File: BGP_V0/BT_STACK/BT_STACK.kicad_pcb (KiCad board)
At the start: 2 copper layers, 30 x 30 mm, 13 parts, among them P1 CONN_01X05, U1 OPA180

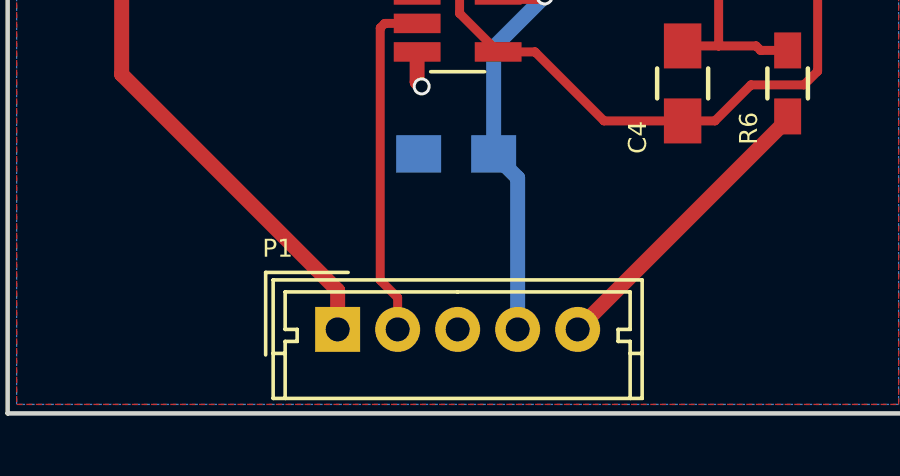
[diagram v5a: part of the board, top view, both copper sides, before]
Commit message: Slight changes to Port layer placement - gerbers done
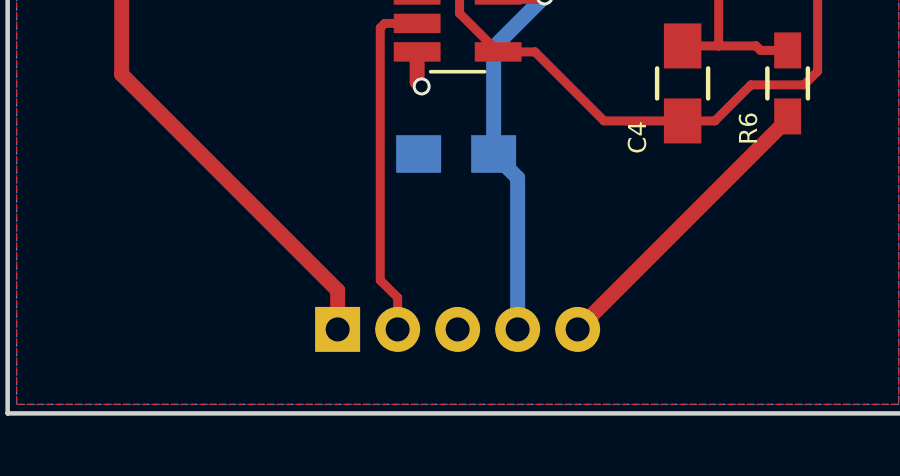
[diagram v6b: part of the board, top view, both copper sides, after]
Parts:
- P1: moved to B.Cu
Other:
- board text added: "+"
- board text added: "-"
- board text added: "G"
- board text added: "I"
- board text added: "O"
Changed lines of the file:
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@@
-(kicad_pcb (version 4) (host pcbnew 4.0.7)
+(kicad_pcb (version 4) (host pcbnew 4.0.4-1.fc24-product)
   (general
     (links 22)
     (no_connects 0)
-    (area 169.924999 67.424999 200.075001 99.455)
+    (area 169.924999 67.424999 200.075001 98.075001)
     (thickness 1.6)
-    (drawings 9)
+    (drawings 14)
     (tracks 80)
     (zones 0)
@@
     )
   )
-  (module Connectors_Molex:Molex_MicroLatch-53253-0570_05x2.00mm_Straight (layer F.Cu)
+  (module Connectors_Molex:Molex_MicroLatch-53253-0570_05x2.00mm_Straight (layer B.Cu)
     (at 181 95.2)
     (descr "Molex Micro-Latch connector, PN:53253-0570, top entry type, through hole")
     (tags "conn molex micro latch")
-    (fp_text reference P1 (at -2 -2.7) (layer F.SilkS)
-      (effects (font (size 0.6 0.6) (thickness 0.15)))
-    )
-    (fp_text value CONN_01X05 (at 4 3.4) (layer F.Fab) hide
-      (effects (font (size 0.6 0.6) (thickness 0.15)))
-    )
-    (fp_line (start -2 -1.5) (end -2 2.15) (layer F.Fab) (width 0.1))
-    (fp_line (start -2 2.15) (end 10 2.15) (layer F.Fab) (width 0.1))
-    (fp_line (start 10 2.15) (end 10 -1.5) (layer F.Fab) (width 0.1))
-    (fp_line (start 10 -1.5) (end -2 -1.5) (layer F.Fab) (width 0.1))
-    (fp_line (start -2.6 -2.1) (end -2.6 2.75) (layer F.CrtYd) (width 0.05))
-    (fp_line (start -2.6 2.75) (end 10.65 2.75) (layer F.CrtYd) (width 0.05))
-    (fp_line (start 10.65 2.75) (end 10.65 -2.1) (layer F.CrtYd) (width 0.05))
-    (fp_line (start 10.65 -2.1) (end -2.6 -2.1) (layer F.CrtYd) (width 0.05))
-    (fp_line (start -2.15 -1.65) (end -2.15 2.3) (layer F.SilkS) (width 0.12))
-    (fp_line (start -2.15 2.3) (end 10.15 2.3) (layer F.SilkS) (width 0.12))
-    (fp_line (start 10.15 2.3) (end 10.15 -1.65) (layer F.SilkS) (width 0.12))
-    (fp_line (start 10.15 -1.65) (end -2.15 -1.65) (layer F.SilkS) (width 0.12))
-    (fp_line (start 0.35 -1.9) (end -2.4 -1.9) (layer F.SilkS) (width 0.12))
-    (fp_line (start -2.4 -1.9) (end -2.4 0.85) (layer F.SilkS) (width 0.12))
-    (fp_line (start 0.35 -1.9) (end -2.4 -1.9) (layer F.Fab) (width 0.1))
-    (fp_line (start -2.4 -1.9) (end -2.4 0.85) (layer F.Fab) (width 0.1))
-    (fp_line (start -2.15 0.8) (end -1.75 0.8) (layer F.SilkS) (width 0.12))
-    (fp_line (start 10.15 0.8) (end 9.75 0.8) (layer F.SilkS) (width 0.12))
-    (fp_line (start 4 -1.25) (end -1.75 -1.25) (layer F.SilkS) (width 0.12))
-    (fp_line (start -1.75 -1.25) (end -1.75 0) (layer F.SilkS) (width 0.12))
-    (fp_line (start -1.75 0) (end -1.35 0) (layer F.SilkS) (width 0.12))
-    (fp_line (start -1.35 0) (end -1.35 0.4) (layer F.SilkS) (width 0.12))
-    (fp_line (start -1.35 0.4) (end -1.75 0.4) (layer F.SilkS) (width 0.12))
-    (fp_line (start -1.75 0.4) (end -1.75 2.3) (layer F.SilkS) (width 0.12))
-    (fp_line (start 4 -1.25) (end 9.75 -1.25) (layer F.SilkS) (width 0.12))
-    (fp_line (start 9.75 -1.25) (end 9.75 0) (layer F.SilkS) (width 0.12))
-    (fp_line (start 9.75 0) (end 9.35 0) (layer F.SilkS) (width 0.12))
-    (fp_line (start 9.35 0) (end 9.35 0.4) (layer F.SilkS) (width 0.12))
-    (fp_line (start 9.35 0.4) (end 9.75 0.4) (layer F.SilkS) (width 0.12))
-    (fp_line (start 9.75 0.4) (end 9.75 2.3) (layer F.SilkS) (width 0.12))
-    (fp_text user %R (at 4 1.5) (layer F.Fab) hide
-      (effects (font (size 0.6 0.6) (thickness 0.15)))
+    (fp_text reference P1 (at 11 -1.85) (layer B.SilkS)
+      (effects (font (size 0.6 0.6) (thickness 0.15)) (justify mirror))
+    )
+    (fp_text value CONN_01X05 (at 4 -3.4) (layer B.Fab) hide
+      (effects (font (size 0.6 0.6) (thickness 0.15)) (justify mirror))
+    )
+    (fp_line (start -2 1.5) (end -2 -2.15) (layer B.Fab) (width 0.1))
+    (fp_line (start -2 -2.15) (end 10 -2.15) (layer B.Fab) (width 0.1))
+    (fp_line (start 10 -2.15) (end 10 1.5) (layer B.Fab) (width 0.1))
+    (fp_line (start 10 1.5) (end -2 1.5) (layer B.Fab) (width 0.1))
+    (fp_line (start -2.6 2.1) (end -2.6 -2.75) (layer B.CrtYd) (width 0.05))
+    (fp_line (start -2.6 -2.75) (end 10.65 -2.75) (layer B.CrtYd) (width 0.05))
+    (fp_line (start 10.65 -2.75) (end 10.65 2.1) (layer B.CrtYd) (width 0.05))
+    (fp_line (start 10.65 2.1) (end -2.6 2.1) (layer B.CrtYd) (width 0.05))
+    (fp_line (start -2.15 1.65) (end -2.15 -2.3) (layer B.SilkS) (width 0.12))
+    (fp_line (start -2.15 -2.3) (end 10.15 -2.3) (layer B.SilkS) (width 0.12))
+    (fp_line (start 10.15 -2.3) (end 10.15 1.65) (layer B.SilkS) (width 0.12))
+    (fp_line (start 10.15 1.65) (end -2.15 1.65) (layer B.SilkS) (width 0.12))
+    (fp_line (start 0.35 1.9) (end -2.4 1.9) (layer B.SilkS) (width 0.12))
+    (fp_line (start -2.4 1.9) (end -2.4 -0.85) (layer B.SilkS) (width 0.12))
+    (fp_line (start 0.35 1.9) (end -2.4 1.9) (layer B.Fab) (width 0.1))
+    (fp_line (start -2.4 1.9) (end -2.4 -0.85) (layer B.Fab) (width 0.1))
+    (fp_line (start -2.15 -0.8) (end -1.75 -0.8) (layer B.SilkS) (width 0.12))
+    (fp_line (start 10.15 -0.8) (end 9.75 -0.8) (layer B.SilkS) (width 0.12))
+    (fp_line (start 4 1.25) (end -1.75 1.25) (layer B.SilkS) (width 0.12))
+    (fp_line (start -1.75 1.25) (end -1.75 0) (layer B.SilkS) (width 0.12))
+    (fp_line (start -1.75 0) (end -1.35 0) (layer B.SilkS) (width 0.12))
+    (fp_line (start -1.35 0) (end -1.35 -0.4) (layer B.SilkS) (width 0.12))
+    (fp_line (start -1.35 -0.4) (end -1.75 -0.4) (layer B.SilkS) (width 0.12))
+    (fp_line (start -1.75 -0.4) (end -1.75 -2.3) (layer B.SilkS) (width 0.12))
+    (fp_line (start 4 1.25) (end 9.75 1.25) (layer B.SilkS) (width 0.12))
+    (fp_line (start 9.75 1.25) (end 9.75 0) (layer B.SilkS) (width 0.12))
+    (fp_line (start 9.75 0) (end 9.35 0) (layer B.SilkS) (width 0.12))
+    (fp_line (start 9.35 0) (end 9.35 -0.4) (layer B.SilkS) (width 0.12))
+    (fp_line (start 9.35 -0.4) (end 9.75 -0.4) (layer B.SilkS) (width 0.12))
+    (fp_line (start 9.75 -0.4) (end 9.75 -2.3) (layer B.SilkS) (width 0.12))
+    (fp_text user %R (at 4 -1.5) (layer B.Fab) hide
+      (effects (font (size 0.6 0.6) (thickness 0.15)) (justify mirror))
     )
     (pad 1 thru_hole rect (at 0 0) (size 1.5 1.5) (drill 0.8) (layers *.Cu *.Mask)
@@
     )
   )
+  (gr_text O (at 189 92) (layer B.SilkS)
+    (effects (font (size 0.6 0.6) (thickness 0.15)) (justify mirror))
+  )
+  (gr_text + (at 187 92) (layer B.SilkS)
+    (effects (font (size 0.6 0.6) (thickness 0.15)) (justify mirror))
+  )
+  (gr_text G (at 185.05 92) (layer B.SilkS)
+    (effects (font (size 0.6 0.6) (thickness 0.15)) (justify mirror))
+  )
+  (gr_text - (at 183 92) (layer B.SilkS)
+    (effects (font (size 0.6 0.6) (thickness 0.15)) (justify mirror))
+  )
+  (gr_text I (at 180.5 92) (layer B.SilkS)
+    (effects (font (size 0.6 0.6) (thickness 0.15)) (justify mirror))
+  )
   (gr_text "BGP V0.0\nB/T Stack" (at 196 70) (layer B.SilkS)

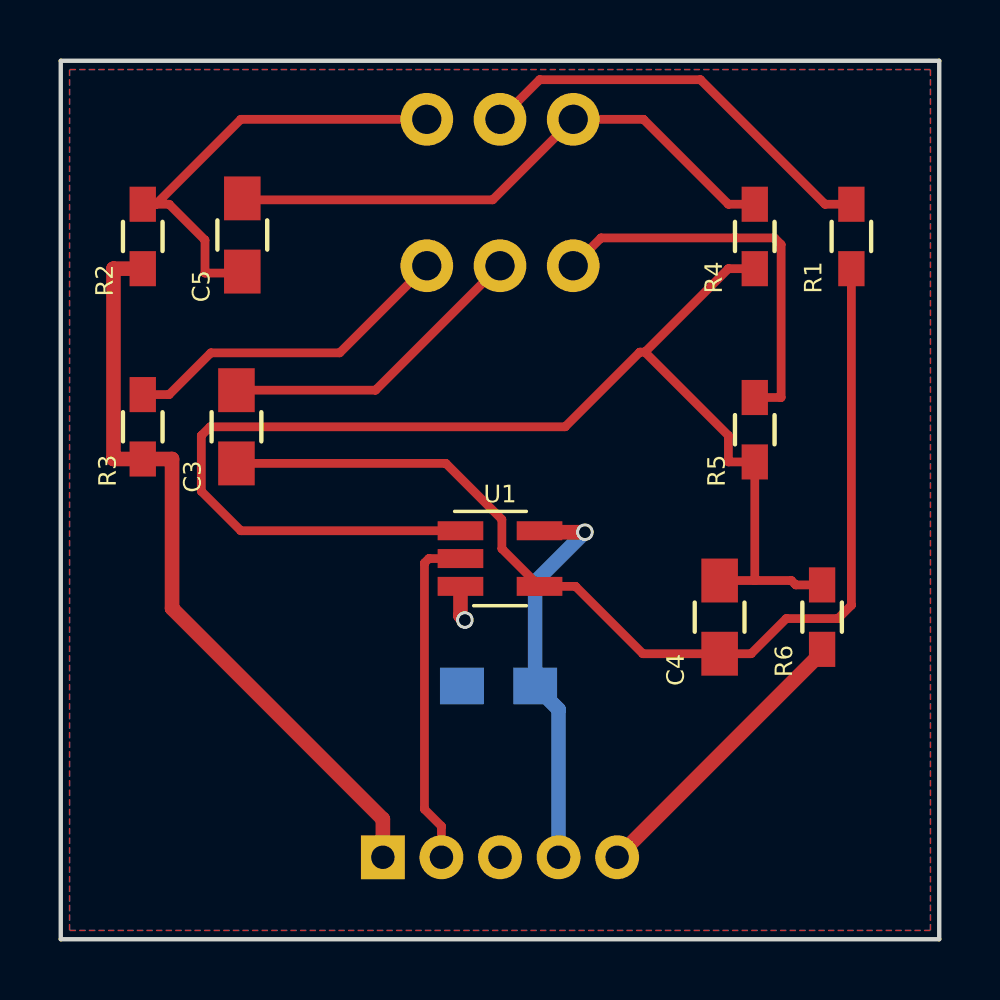
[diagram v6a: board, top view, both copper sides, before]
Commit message: Reduced BT MID board sizes.
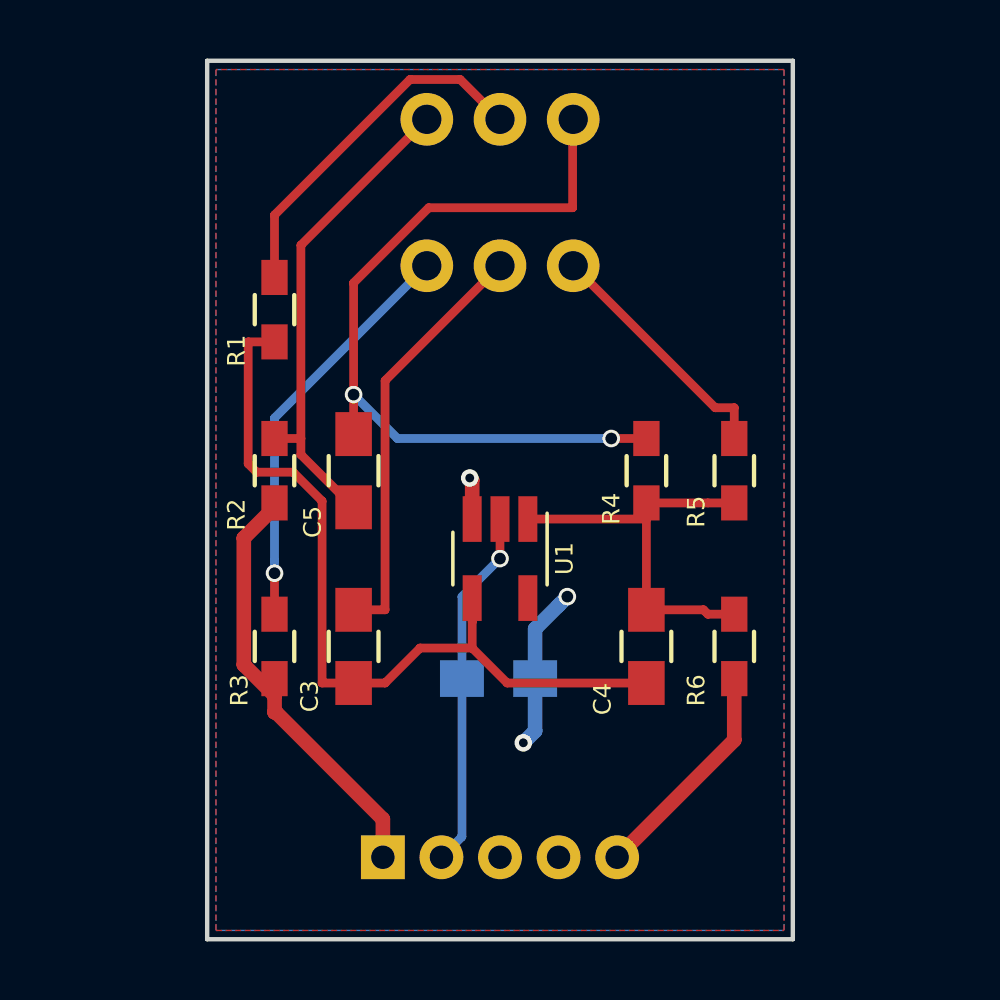
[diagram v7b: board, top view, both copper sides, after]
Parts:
- moved R1 19.9 mm to (177.3, 76.5)
- moved R2 9.18 mm to (177.3, 82.0)
- moved C5 8.90 mm to (180.0, 82.0)
- moved R4 8.81 mm to (190.0, 82.0)
- moved R3 8.75 mm to (177.3, 88.0)
- moved C3 8.50 mm to (180.0, 88.0)
- moved R6 3.16 mm to (193.0, 88.0)
- moved C4 2.69 mm to (190.0, 88.0)
- moved R5 1.57 mm to (193.0, 82.0)
- moved C1 0.25 mm to (184.9, 89.1)
- turned U1 to 270 degrees
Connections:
- C1 pad 2: Net-(C1-Pad2) -> /V-
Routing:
- net Net-(C4-Pad1): track 46.0 -> 13.8 mm
- net /IN: track 26.1 -> 15.1 mm
- net Net-(C3-Pad2): track 36.5 -> 28.1 mm
- net /V+: track 13.7 -> 5.61 mm, vias 1 -> 2
- net /B+: track 20.0 -> 27.4 mm, vias 0 -> 2
- net /T+: track 13.7 -> 8.56 mm
- net /TW: track 10.8 -> 14.5 mm
- net /T-: track 11.5 -> 14.1 mm, vias 0 -> 1
- net /OUT: track 10.00 -> 7.76 mm
- net /BW: track 14.3 -> 12.3 mm
- net /B-: track 15.3 -> 16.7 mm
- net /V-: track 11.6 -> 12.5 mm, vias 0 -> 1
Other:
- board size 30 x 30 mm -> 20 x 30 mm
